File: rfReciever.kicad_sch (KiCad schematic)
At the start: 33 parts, among them J1 MOLEX 1054440001, SW1 RF_RESET, SW2 RF_SLEEP, U2 USBLC6-2SC6, U3 FT234XD-R, U4 TPS76333DBVT, X1 DigiXBeeRX900Micro

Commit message: schematic mk2 post matthew review
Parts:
- removed R1: 10K, Resistor_SMD:R_0805_2012Metric, symbol Device:R
- added C2, C3, C4: 0.1uF, Capacitor_SMD:C_0805_2012Metric, symbol Device:C
- added L1: 4.7 uH, Inductor_SMD:L_0805_2012Metric, symbol Device:L
- C1: footprint (none) -> Capacitor_SMD:C_0805_2012Metric
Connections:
- net +3.3V: no longer U3.3 (3V3OUT), U3.4 (VCC), U3.9 (VCCIO)
- net +5V: now also C1.1, U2.5 (VBUS), L1.2
- net GND: now also C2.2, C3.2, C4.2; no longer U2.5 (VBUS)
- net FTDI_3.3V: now reaches U3.2 (~{RESET}#)
- net FTDI_3.3V: now also U3.3 (3V3OUT), U3.9 (VCCIO), C2.1, C3.1; no longer C1.1
- new net FTDI_VCC: C4.1, L1.1, U3.4 (VCC)

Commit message: gitignore + layout v3 + routing
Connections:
- net VCCIO is gone; now on net FTDI_3.3V: U3.6 (CBUS0)
- net USBDP: now reaches R19.1, U3.12 (USBDP)
- net USBDM: now reaches R14.1, U3.1 (USBDM)
- net MLX(D+) renamed MLXDP
- net MLX(D-) renamed MLXDN
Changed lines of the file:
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@@
 	(wire
 		(pts
-			(xy 177.8 195.58) (xy 177.8 199.39)
+			(xy 177.8 196.85) (xy 177.8 199.39)
 		)
 		(stroke
@@
 		)
 	)
+	(label "USBDM"
+		(at 220.98 209.55 0)
+		(fields_autoplaced yes)
+		(effects
+			(font
+				(size 1.27 1.27)
+			)
+			(justify left bottom)
+		)
+	)
 	(label "RF_TXD"
 		(at 309.88 62.23 0)
@@
 	)
 	(label "FTDI_3.3V"
-		(at 177.8 195.58 0)
+		(at 177.8 196.85 0)
 		(fields_autoplaced yes)
 		(effects
@@
 		)
 	)
+	(label "FTDI_RESET"
+		(at 177.8 201.93 0)
+		(fields_autoplaced yes)
+		(effects
+			(font
+				(size 1.27 1.27)
+			)
+			(justify left bottom)
+		)
+	)
 	(label "RF_D9"
 		(at 328.93 120.65 0)
@@
 		)
 	)
-	(label "MLX(D+)"
+	(label "MLXDP"
 		(at 29.21 72.39 0)
 		(fields_autoplaced yes)
@@
 		)
 	)
+	(label "USBDP"
+		(at 220.98 212.09 0)
+		(fields_autoplaced yes)
+		(effects
+			(font
+				(size 1.27 1.27)
+			)
+			(justify left bottom)
+		)
+	)
 	(label "MLX(VBUS)"
 		(at 151.13 191.77 0)
@@
 		)
 	)
-	(label "MLX(D-)"
+	(label "MLXDN"
 		(at 113.03 95.25 0)
 		(fields_autoplaced yes)
@@
 		)
 	)
-	(label "MLX(D-)"
+	(label "MLXDN"
 		(at 29.21 74.93 0)
 		(fields_autoplaced yes)
@@
 		)
 	)
-	(label "MLX(D+)"
+	(label "VCCIO"
+		(at 222.25 201.93 0)
+		(fields_autoplaced yes)
+		(effects
+			(font
+				(size 1.27 1.27)
+			)
+			(justify left bottom)
+		)
+	)
+	(label "MLXDP"
 		(at 113.03 100.33 0)
 		(fields_autoplaced yes)

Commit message: revisions requested by Lakshay, new LDO
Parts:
- removed C1: 10nF, Capacitor_SMD:C_0805_2012Metric, symbol Device:C
- removed C3, C4: 0.1uF, Capacitor_SMD:C_0805_2012Metric, symbol Device:C
- removed L1: 4.7 uH, Inductor_SMD:L_0805_2012Metric, symbol Device:L
- removed U4: TPS76333DBVT, rfReciever-Footprints:SOT95P280X145-5N, symbol ExternalLDO:TPS76333DBVT
- added C12, C13: 47pF, Capacitor_SMD:C_0805_2012Metric, symbol Device:C
- added U1: TLV70130DBVR, rfReciever-Footprints:DBV5, symbol FinalLDO:TLV70130DBVR
- C11: value 4.7uF -> 1uF
- C2: value 0.1uF -> 100nF
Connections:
- net FTDI_VCC is gone; now on net +3.3V: U3.4 (VCC)
- net +3.3V: now also U1.1 (OUT)
- net +5V: now also U1.3 (IN)
- net GND: now also C12.2, C13.2, U1.2 (GND)
- net USB_OUT_D+: now also C13.1
- net USB_OUT_D-: now also C12.1
- net FTDI_3.3V renamed FTDI_RESET
- net FTDI_RESET: no longer U3.6 (CBUS0)
- no-connect marks 23 -> 26
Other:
- moved on the sheet: R14, R19, U3

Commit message: reworked layout slightly + 3d models
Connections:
- net MLXDN renamed USBMLXDN
- net MLXDP renamed USBMLXDP
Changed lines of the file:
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@@
 		)
 	)
-	(label "MLXDP"
+	(label "USBMLXDP"
 		(at 29.21 72.39 0)
 		(fields_autoplaced yes)
@@
 		)
 	)
-	(label "MLXDN"
+	(label "USBMLXDN"
 		(at 113.03 95.25 0)
 		(fields_autoplaced yes)
@@
 		)
 	)
-	(label "MLXDN"
+	(label "USBMLXDN"
 		(at 29.21 74.93 0)
 		(fields_autoplaced yes)
@@
 		)
 	)
-	(label "MLXDP"
+	(label "USBMLXDP"
 		(at 113.03 100.33 0)
 		(fields_autoplaced yes)

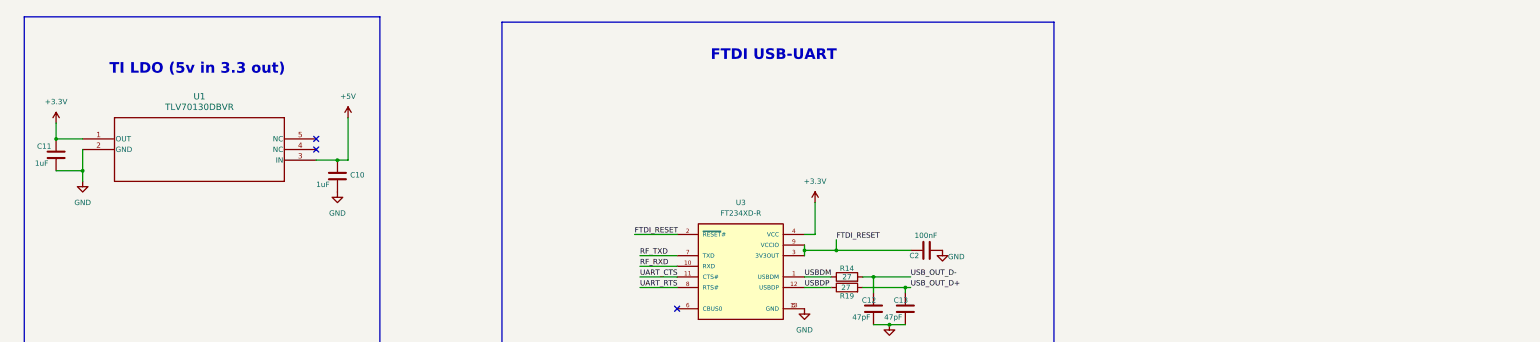
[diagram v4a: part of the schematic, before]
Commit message: added testpoints, TODO: Ground pours + ground conn
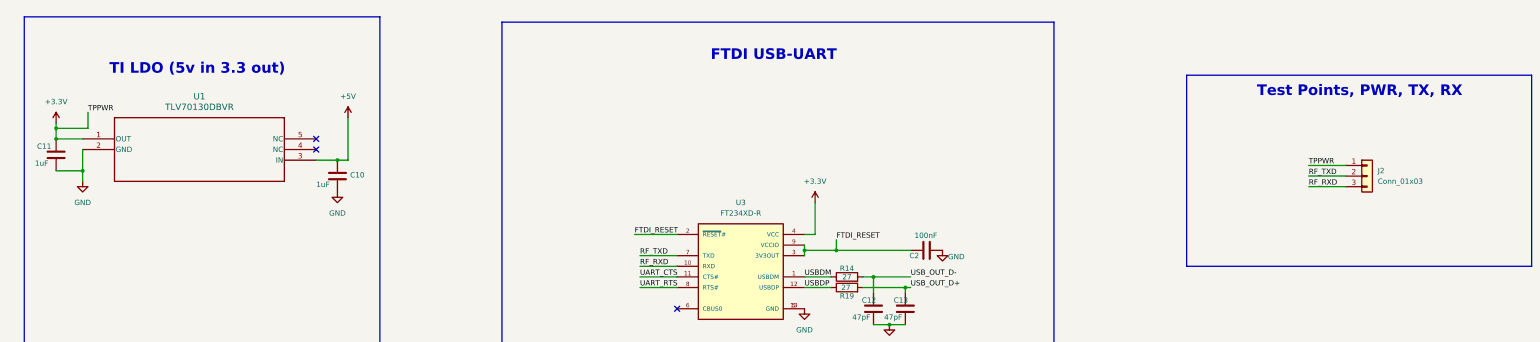
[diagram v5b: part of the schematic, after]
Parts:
- added J2: Conn_01x03, Connector_PinHeader_2.54mm:PinHeader_1x03_P2.54mm_Vertical, symbol Connector_Generic:Conn_01x03
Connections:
- net +3.3V: now also J2.1 (Pin_1)
- net RF_RXD: now also J2.3 (Pin_3)
- net RF_TXD: now also J2.2 (Pin_2)
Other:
- note added: "Test Points, PWR, TX, RX"
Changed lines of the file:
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@@
 	)
 	(junction
+		(at 29.21 180.34)
+		(diameter 0)
+		(color 0 0 0 0)
+	)
+	(junction
 		(at 213.36 54.61)
 		(diameter 0)
@@
 	(wire
 		(pts
+			(xy 29.21 180.34) (xy 29.21 182.88)
+		)
+		(stroke
+			(width 0)
+			(type default)
+		)
+	)
+	(wire
+		(pts
 			(xy 234.95 54.61) (xy 247.65 54.61)
 		)
@@
 	(wire
 		(pts
+			(xy 29.21 180.34) (xy 36.83 180.34)
+		)
+		(stroke
+			(width 0)
+			(type default)
+		)
+	)
+	(wire
+		(pts
 			(xy 168.91 215.9) (xy 177.8 215.9)
 		)
@@
 	(wire
 		(pts
+			(xy 328.93 189.23) (xy 337.82 189.23)
+		)
+		(stroke
+			(width 0)
+			(type default)
+		)
+	)
+	(wire
+		(pts
 			(xy 142.24 100.33) (xy 142.24 99.06)
 		)
@@
 	(wire
 		(pts
-			(xy 29.21 179.07) (xy 29.21 182.88)
+			(xy 29.21 179.07) (xy 29.21 180.34)
+		)
+		(stroke
+			(width 0)
+			(type default)
+		)
+	)
+	(wire
+		(pts
+			(xy 328.93 191.77) (xy 337.82 191.77)
 		)
 		(stroke
@@
 	(wire
 		(pts
+			(xy 36.83 176.53) (xy 36.83 180.34)
+		)
+		(stroke
+			(width 0)
+			(type default)
+		)
+	)
+	(wire
+		(pts
 			(xy 29.21 74.93) (xy 39.37 74.93)
 		)
@@
 	(wire
 		(pts
+			(xy 328.93 194.31) (xy 337.82 194.31)
+		)
+		(stroke
+			(width 0)
+			(type default)
+		)
+	)
+	(wire
+		(pts
 			(xy 318.77 132.08) (xy 318.77 128.27)
 		)
@@
 	)
 	(rectangle
+		(start 299.72 167.64)
+		(end 382.27 213.36)
+		(stroke
+			(width 0)
+			(type default)
+		)
+		(fill
+			(type none)
+		)
+	)
+	(rectangle
 		(start 21.59 153.67)
 		(end 106.68 266.7)
@@
 		)
 	)
+	(text "Test Points, PWR, TX, RX"
+		(exclude_from_sim no)
+		(at 341.122 171.45 0)
+		(effects
+			(font
+				(size 2.54 2.54)
+				(thickness 0.508)
+				(bold yes)
+			)
+		)
+	)
 	(text "TI LDO (5v in 3.3 out)"
 		(exclude_from_sim no)
@@
 		)
 	)
+	(label "TPPWR"
+		(at 328.93 189.23 0)
+		(fields_autoplaced yes)
+		(effects
+			(font
+				(size 1.27 1.27)
+			)
+			(justify left bottom)
+		)
+	)
 	(label "USB_OUT_D+"
 		(at 144.78 100.33 0)
@@
 		)
 	)
+	(label "TPPWR"
+		(at 36.83 176.53 0)
+		(fields_autoplaced yes)
+		(effects
+			(font
+				(size 1.27 1.27)
+			)
+			(justify left bottom)
+		)
+	)
 	(label "RF_SW_RESET"
 		(at 347.98 80.01 0)
@@
 	)
 	(label "RF_RXD"
+		(at 328.93 194.31 0)
+		(fields_autoplaced yes)
+		(effects
+			(font
+				(size 1.27 1.27)
+			)
+			(justify left bottom)
+		)
+	)
+	(label "RF_TXD"
+		(at 328.93 191.77 0)
+		(fields_autoplaced yes)
+		(effects
+			(font
+				(size 1.27 1.27)
+			)
+			(justify left bottom)
+		)
+	)
+	(label "RF_RXD"
 		(at 168.91 213.36 0)
 		(fields_autoplaced yes)
@@
 					(unit 1)
 				)
+			)
+		)
+	)
+	(symbol
+		(lib_id "Connector_Generic:Conn_01x03")
+		(at 342.9 191.77 0)
+		(unit 1)
+		(exclude_from_sim no)
+		(in_bom yes)
+		(on_board yes)
+		(dnp no)
+		(fields_autoplaced yes)
+		(property "Reference" "J2"
+			(at 345.44 190.4999 0)
+			(effects
+				(font
+					(size 1.27 1.27)
+				)
+				(justify left)
+			)
+		)
+		(property "Value" "Conn_01x03"
+			(at 345.44 193.0399 0)
+			(effects
+				(font
+					(size 1.27 1.27)
+				)
+				(justify left)
+			)
+		)
+		(property "Footprint" "Connector_PinHeader_2.54mm:PinHeader_1x03_P2.54mm_Vertical"
+			(at 342.9 191.77 0)
+			(effects
+				(font
+					(size 1.27 1.27)
+				)
+				(hide yes)
+			)
+		)
+		(property "Datasheet" "~"
+			(at 342.9 191.77 0)
+			(effects
+				(font
+					(size 1.27 1.27)
+				)
+				(hide yes)
+			)
+		)
+		(property "Description" "Generic connector, single row, 01x03, script generated (kicad-library-utils/schlib/autogen/connector/)"
+			(at 342.9 191.77 0)
+			(effects
+				(font
+					(size 1.27 1.27)
+				)
+				(hide yes)
+			)
+		)
+		(pin "1"
+		)
+		(pin "2"
+		)
+		(pin "3"
+		)
+		(instances
+			(project ""
+				(path "/1c5a3368-abed-417b-9a38-92624a95b87f"
+					(reference "J2")
+					(unit 1)
+				)

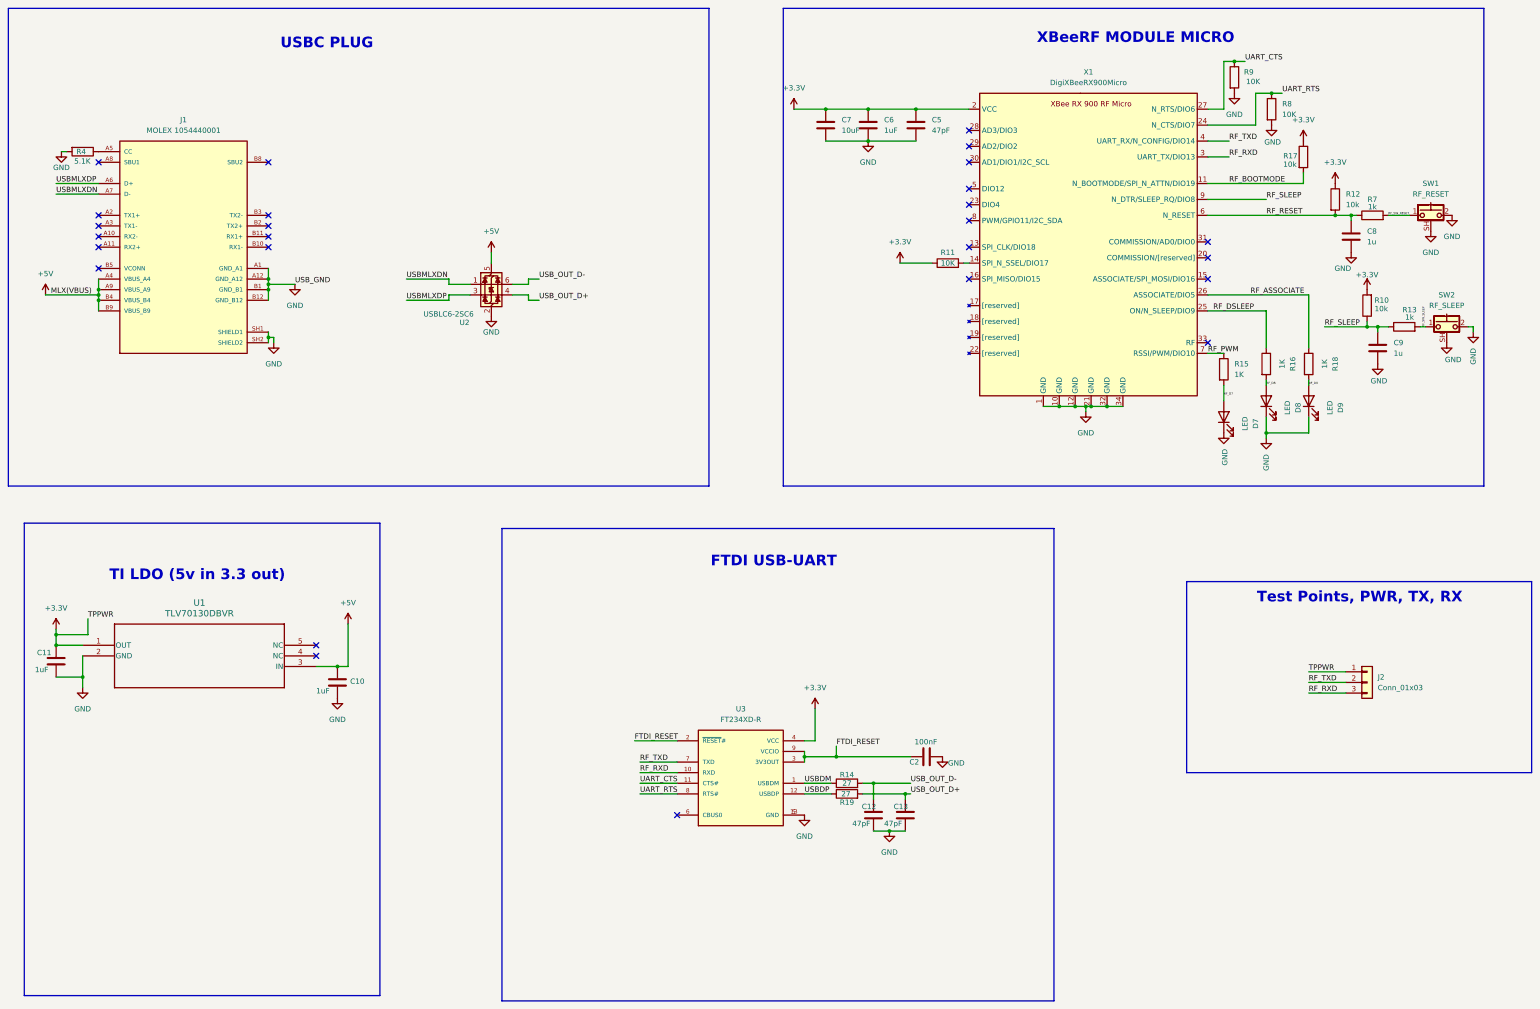
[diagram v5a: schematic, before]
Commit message: Minor updates (test points, silkscreen, traces)
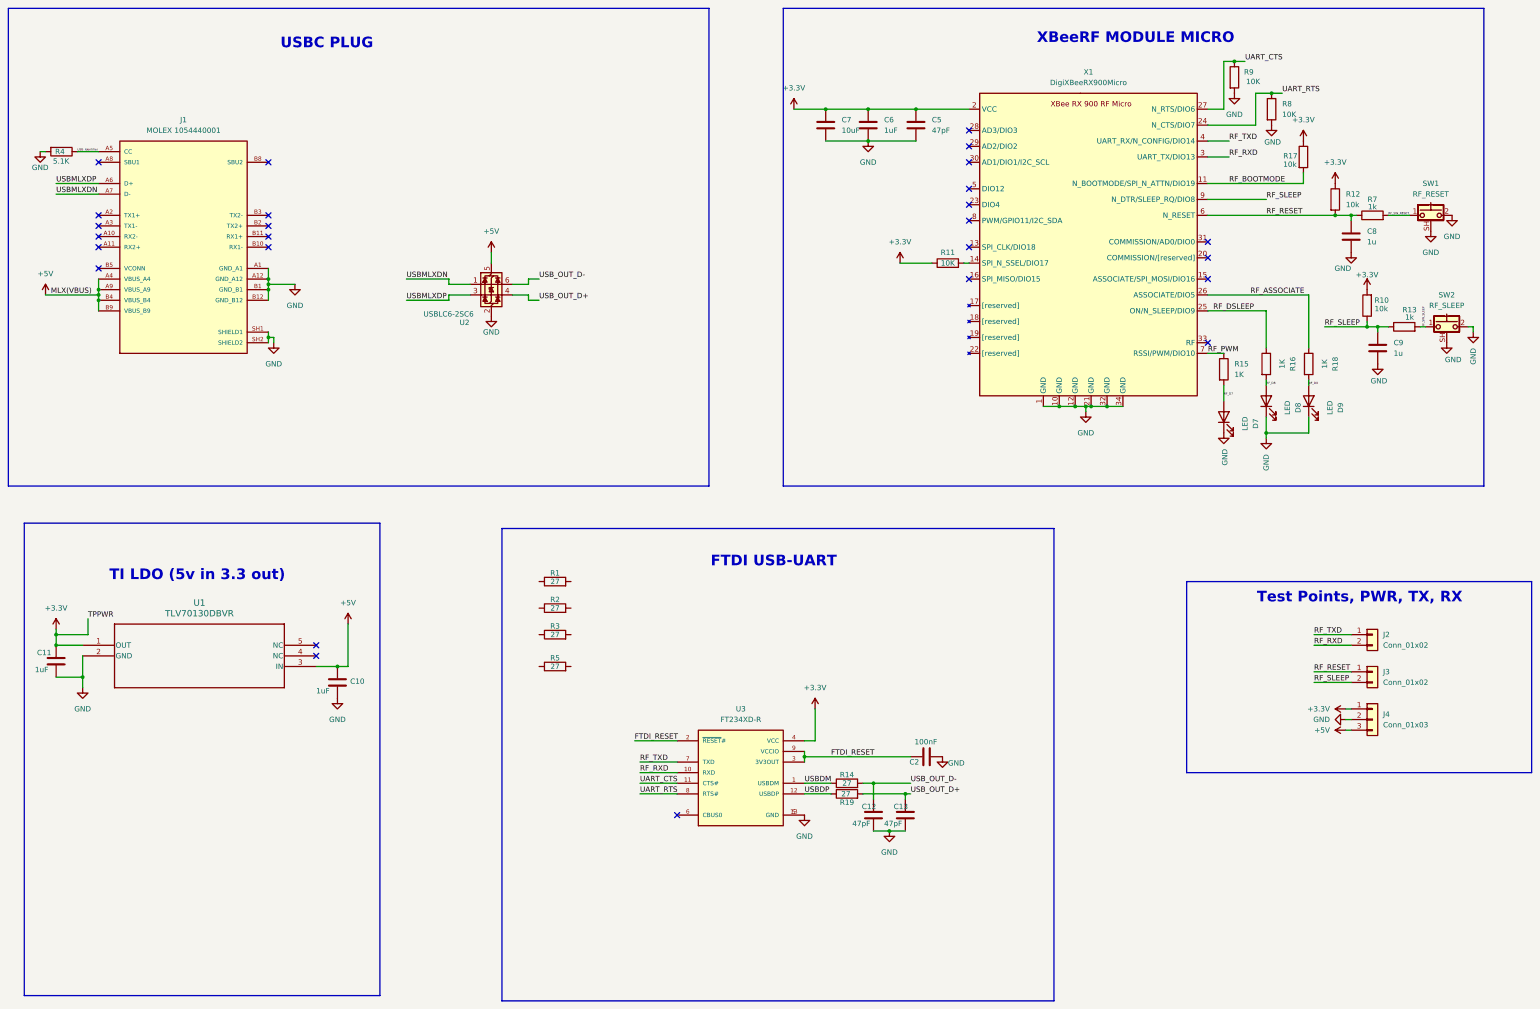
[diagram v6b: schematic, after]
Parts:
- removed J2: Conn_01x03, Connector_PinHeader_2.54mm:PinHeader_1x03_P2.54mm_Vertical, symbol Connector_Generic:Conn_01x03
- added J2, J3: Conn_01x02, Connector_PinHeader_2.00mm:PinHeader_1x02_P2.00mm_Vertical_SMD_Pin1Left, symbol Connector_Generic:Conn_01x02
- added J4: Conn_01x03, Connector_PinHeader_2.54mm:PinHeader_1x03_P2.54mm_Vertical, symbol Connector_Generic:Conn_01x03
- added R1: 27, rfReciever-Footprints:stockBroker, symbol Device:R
- added R2: 27, rfReciever-Footprints:RFHazard, symbol Device:R
- added R3: 27, rfReciever-Footprints:dataNetwork, symbol Device:R
- added R5: 27, rfReciever-Footprints:emWave, symbol Device:R
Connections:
- net +3.3V: now also J4.1 (Pin_1)
- net +5V: now also J4.3 (Pin_3)
- net GND: now also J4.2 (Pin_2)
- net RF_RESET: now also J3.1 (Pin_1)
- net RF_RXD: now also J2.2 (Pin_2)
- net RF_SLEEP: now also J3.2 (Pin_2)
- net RF_TXD: now also J2.1 (Pin_1)
- net USB_Identifier: now reaches J1.A5 (CC), R4.1
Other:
- moved on the sheet: R4
